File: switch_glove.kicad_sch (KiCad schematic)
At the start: 82 parts, among them J1 MSD-4-A, J2 USB4105GFA120, Q1 DSG, Q2 CHG, SW1 BATSW, U1 ESP32-D0WD-V3, U2 TPS62162DSG, U3 IS25LP032D-JBLE-TR, U4 BQ29700DSER, U5 BQ25895RTWR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

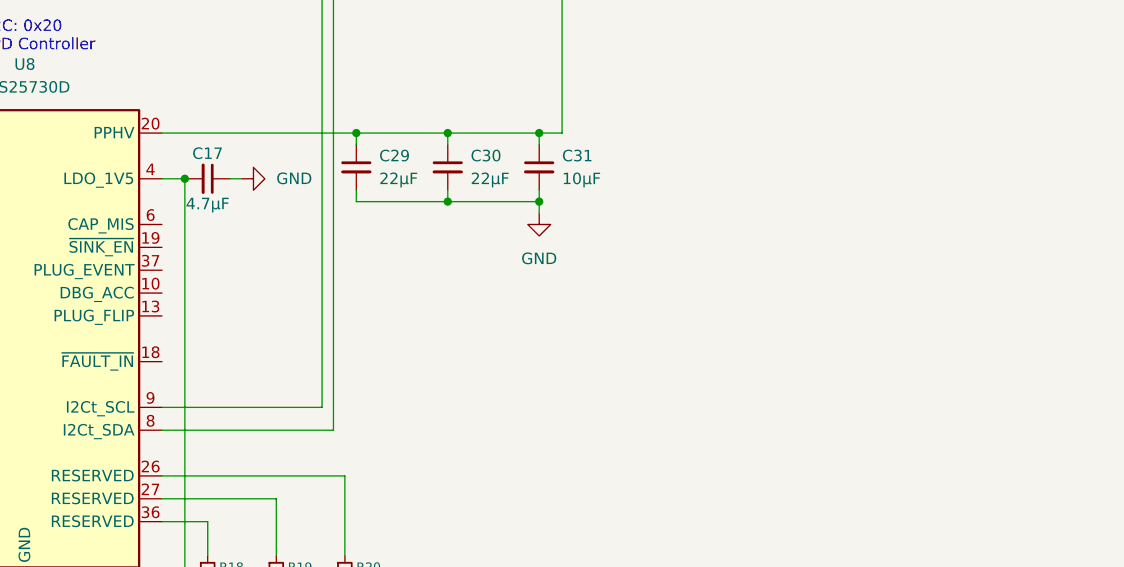
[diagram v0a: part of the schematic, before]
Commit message: Finished USB-PD Controller
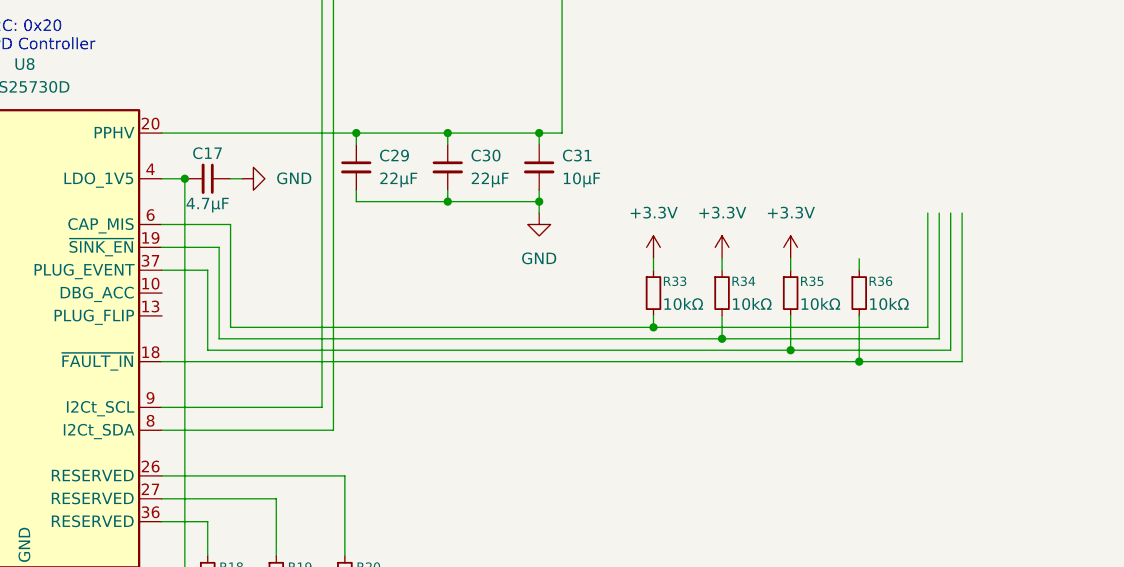
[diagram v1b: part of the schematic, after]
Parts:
- added R33, R34, R35, R36: 10kΩ, symbol Device:R_Small
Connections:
- net +3.3V: now also R33.1, R34.1, R35.1
- net at U8.18 (~{FAULT_IN}): now also R36.2
- net at U8.19 (~{SINK_EN}): now also R34.2
- net at U8.37 (PLUG_EVENT): now also R35.2
- net at U8.6 (CAP_MIS): now also R33.2

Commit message: Added Buck Converter IC
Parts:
- removed CIN1: 10μF, symbol Device:C_Small
- removed CIN2, COUT2: 0.1μF, symbol Device:C_Small
- removed COUT1: 22μF, symbol Device:C_Small
- removed L1: 2.2μH, symbol Device:L
- removed R17: 100kΩ, symbol Device:R_Small
- removed U2: TPS62162DSG, Package_SON:WSON-8-1EP_2x2mm_P0.5mm_EP0.9x1.6mm_ThermalVias, symbol Regulator_Switching:TPS62162DSG
- added U2: TPS6282533DMQR, DMQ0006A, symbol TPS6282533DMQR:TPS6282533DMQR
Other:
- moved on the sheet: U7

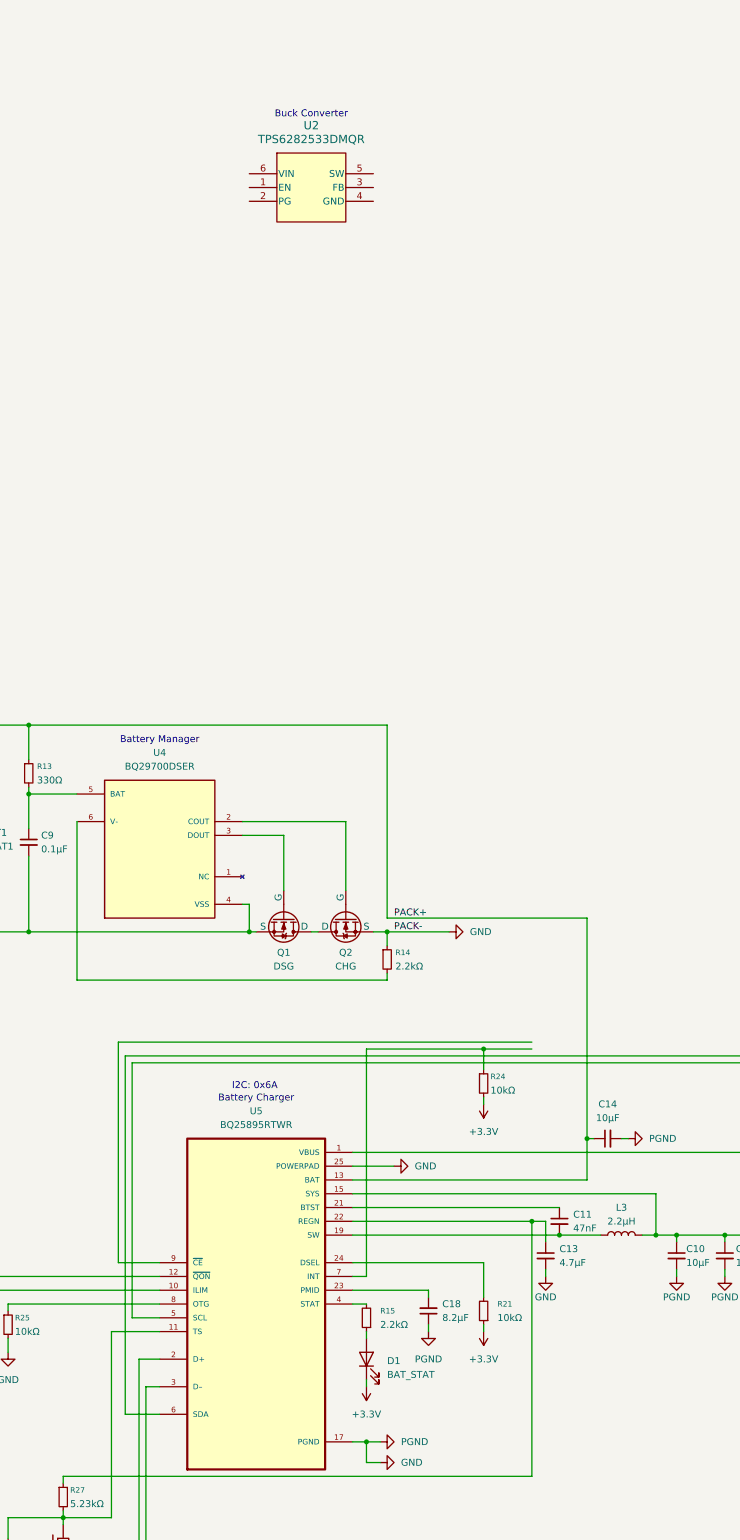
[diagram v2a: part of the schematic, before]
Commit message: Added Buck Wiring
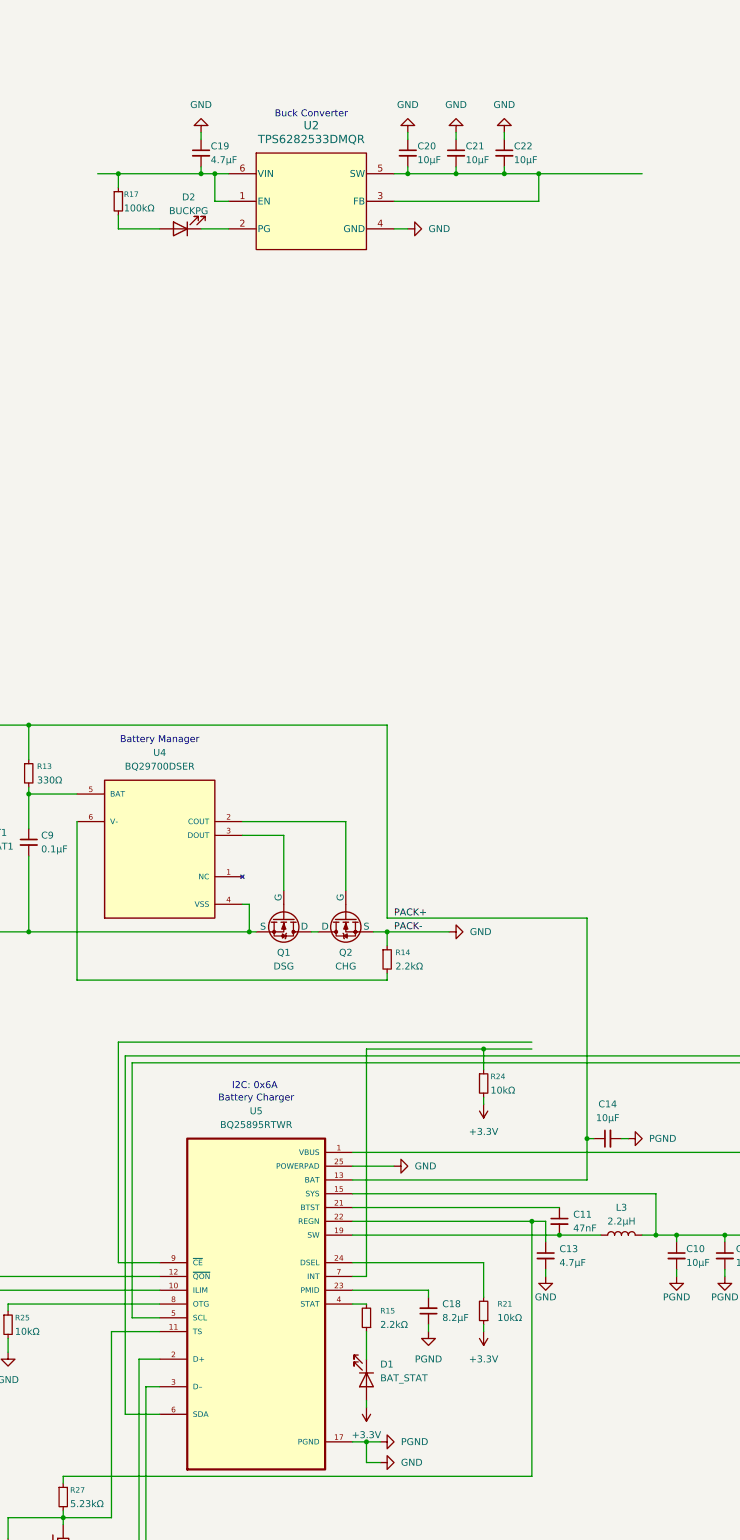
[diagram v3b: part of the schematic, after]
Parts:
- added C19: 4.7µF, symbol Device:C_Small
- added C20, C21, C22: 10µF, symbol Device:C_Small
- added D2: BUCKPG, symbol Device:LED
- added R17: 100kΩ, symbol Device:R_Small
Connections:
- net +3.3V: now also D1.2 (A); no longer D1.1 (K)
- net GND: now also U2.4 (GND), C19.1, C20.1, C21.1, C22.1
- net at R15.1: now also D1.1 (K); no longer D1.2 (A)
- net at U2.1 (EN): now also U2.6 (VIN), C19.2, R17.1
- net at U2.2 (PG): now also D2.1 (K)
- net at U2.3 (FB): now also U2.5 (SW), C20.2, C21.2, C22.2
- new net: D2.2 (A), R17.2
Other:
- moved on the sheet: D1

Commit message: Connected Buck Converter Input to Battery Charger Output
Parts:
- added L1: 1.0µH, 3.5A, symbol Device:L
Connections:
- net +3.3V: now also C20.2, C21.2, C22.2, U2.3 (FB), L1.2
- net SYS: now also C19.2, R17.1, U2.1 (EN), U2.6 (VIN)
- new net: L1.1, U2.5 (SW)
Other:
- moved on the sheet: C15, C16, C17, C19, C20, C21, C22, C23, C24, C25, C26, C27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
